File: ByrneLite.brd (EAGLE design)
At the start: 38.1 x 76.2 mm, 24 parts, among them J1 5V Reg, U1 TINY85, U2 S108T02, U3 S108T02, U4 S108T02

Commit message: Generated gerbers for v1
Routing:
- net N$5: track 12.1 -> 14.7 mm, vias 0 -> 1
- net 5V: track 94.4 -> 96.2 mm
- net GND: track 194.6 -> 195.6 mm

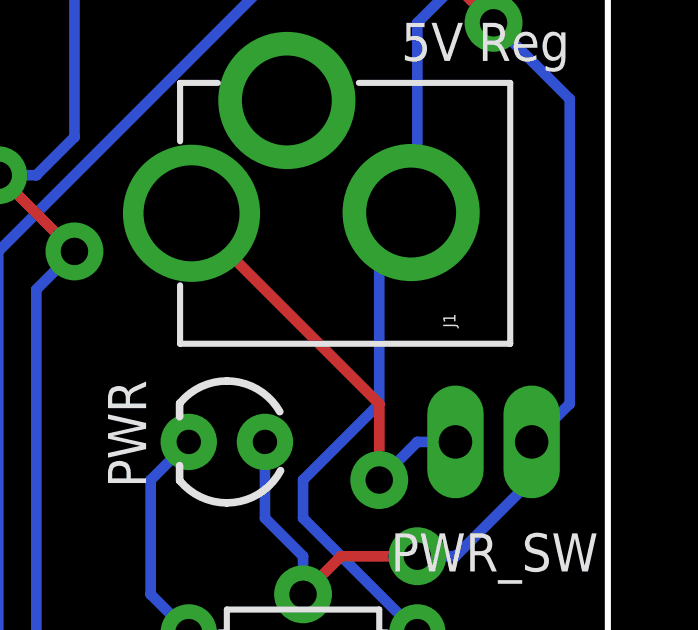
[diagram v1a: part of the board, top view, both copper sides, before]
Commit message: Changed to LGPL license
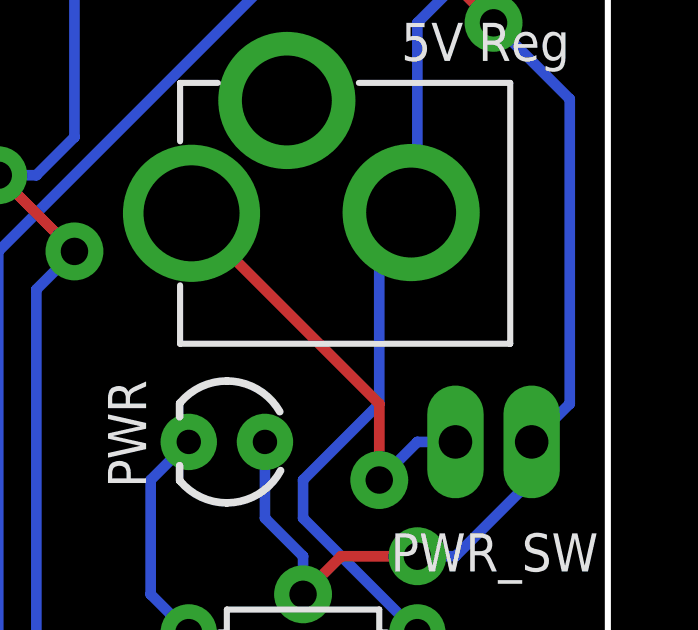
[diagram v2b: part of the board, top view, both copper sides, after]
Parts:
- R12, R3, R8: value 150 -> 330
- R13: value 330 -> 10K
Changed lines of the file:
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@@
 <attribute name="VALUE" x="0.6096" y="6.8834" size="1.27" layer="27" ratio="10" rot="R180"/>
 </element>
-<element name="R3" library="SparkFun" package="AXIAL-0.3" value="150" x="15.24" y="6.35" smashed="yes" rot="R270">
+<element name="R3" library="SparkFun" package="AXIAL-0.3" value="330" x="15.24" y="6.35" smashed="yes" rot="R270">
 <attribute name="NAME" x="16.51" y="8.89" size="0.4064" layer="25" font="vector" rot="R270"/>
 <attribute name="VALUE" x="14.732" y="7.62" size="1.016" layer="27" font="vector" rot="R270"/>
@@
 <attribute name="VALUE" x="0.6096" y="32.2834" size="1.27" layer="27" ratio="10" rot="R180"/>
 </element>
-<element name="R8" library="SparkFun" package="AXIAL-0.3" value="150" x="15.24" y="31.75" smashed="yes" rot="R270">
+<element name="R8" library="SparkFun" package="AXIAL-0.3" value="330" x="15.24" y="31.75" smashed="yes" rot="R270">
 <attribute name="NAME" x="16.51" y="34.29" size="0.4064" layer="25" font="vector" rot="R270"/>
 <attribute name="VALUE" x="14.732" y="33.147" size="1.016" layer="27" font="vector" rot="R270"/>
@@
 <attribute name="VALUE" x="0.6096" y="57.6834" size="1.27" layer="27" ratio="10" rot="R180"/>
 </element>
-<element name="R12" library="SparkFun" package="AXIAL-0.3" value="150" x="15.24" y="57.15" smashed="yes" rot="R270">
+<element name="R12" library="SparkFun" package="AXIAL-0.3" value="330" x="15.24" y="57.15" smashed="yes" rot="R270">
 <attribute name="NAME" x="16.51" y="59.69" size="0.4064" layer="25" font="vector" rot="R270"/>
 <attribute name="VALUE" x="14.732" y="58.42" size="1.016" layer="27" font="vector" rot="R270"/>
@@
 <element name="STANDOFF4" library="SparkFun-Electromechanical" package="STAND-OFF" value="STAND-OFF" x="34.29" y="72.39"/>
 <element name="J1" library="Dek" package="POWER_JACK_PTH_LOCK" value="5V Reg" x="38.1" y="29.21" smashed="yes" rot="R90">
-<attribute name="NAME" x="33.02" y="25.4" size="0.4064" layer="25" rot="R90"/>
+<attribute name="NAME" x="33.02" y="25.4" size="0.4064" layer="27" rot="R90"/>
 <attribute name="VALUE" x="36.83" y="35.56" size="1.27" layer="25" rot="R180"/>
 </element>
@@
 <attribute name="VALUE" x="22.1996" y="23.3934" size="1.27" layer="27" ratio="10" rot="R180"/>
 </element>
-<element name="R13" library="SparkFun" package="AXIAL-0.3" value="330" x="27.94" y="15.24" smashed="yes" rot="R180">
+<element name="R13" library="SparkFun" package="AXIAL-0.3" value="10K" x="27.94" y="15.24" smashed="yes" rot="R180">
 <attribute name="NAME" x="30.48" y="13.97" size="0.4064" layer="25" font="vector" rot="R180"/>
 <attribute name="VALUE" x="29.464" y="15.748" size="1.016" layer="27" font="vector" rot="R180"/>
